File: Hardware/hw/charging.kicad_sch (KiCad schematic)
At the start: 7 parts, among them J1 Screw_Terminal_01x02, J2 Screw_Terminal_01x02, Q2 PMOS, Q3 PMOS, U3 INA219, U7 BQ24650

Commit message: Scheme update
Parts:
- added Q4: PMOS, symbol Simulation_SPICE:PMOS
- added R3: 100k, symbol Device:R
- added R4: 1k, symbol Device:R
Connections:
- net at Q3.3 (S): now also Q4.3 (S), R3.1
- new net: Q4.2 (G), R3.2, R4.1
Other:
- moved on the sheet: U3

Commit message: update
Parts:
- removed U3: INA219, INA219:MODULE_INA219, symbol INA219:INA219
- removed U7: BQ24650, symbol BQ24650:BQ24650
- added J3: Conn_01x05_Pin, Connector_PinSocket_2.54mm:PinSocket_1x05_P2.54mm_Vertical, symbol Connector:Conn_01x05_Pin
- added J5: Conn_01x04_Pin, Connector_PinSocket_2.54mm:PinSocket_1x04_P2.54mm_Vertical, symbol Connector:Conn_01x04_Pin
- added R5, R6: 4k7, symbol Device:R
- added R7, R8: 10k, symbol Device:R
- added SunnyBuddy:PRT-12885: ~, SunnyBuddy:PRT-12885, symbol PRT-12885:Sunny Buddy PRT-12885
- added U3, U8: SMS3.3.TCT, symbol DVIULC6-4SC6:SMS3.3.TCT
- added U7: INA219, INA219_Module:MODULE_INA219, symbol INA219:INA219
- D3: footprint (none) -> SMBJ24CA:DO214AA
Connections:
- net GND: now also J3.5 (Pin_5), J5.4 (Pin_4), SunnyBuddy:PRT-12885.2 (Sol-), SunnyBuddy:PRT-12885.4 (GND), U3.2 (GND), U7.2 (GND), U8.2 (GND)
- net Charging: now reaches R4.2
- net Charging: now also J3.4 (Pin_4), U3.6 (IO4)
- net at J2.1 (Pin_1): now also SunnyBuddy:PRT-12885.7 (LOAD+)
- net at J2.2 (Pin_2): now also SunnyBuddy:PRT-12885.8 (LOAD-)
- net at Q4.1 (D): now also U7.6 (VIN+)
- new net: SunnyBuddy:PRT-12885.1 (Sol+), U7.5 (VIN-)
- new net CHG: J5.3 (Pin_3), R8.2, SunnyBuddy:PRT-12885.6 (CHG), U8.6 (IO4)
- new net FAULT: J5.2 (Pin_2), R7.2, SunnyBuddy:PRT-12885.5 (FAULT), U8.3 (IO2)
- new net SCL: J3.2 (Pin_2), R5.2, U3.1 (IO1), U3.3 (IO2), U7.3 (SCL)
- new net SDA: J3.3 (Pin_3), R6.2, U7.4 (SDA)
- new net SET: J5.1 (Pin_1), SunnyBuddy:PRT-12885.3 (SET), U8.1 (IO1)
- new net VCC: J3.1 (Pin_1), R5.1, R6.1, R7.1, R8.1, U3.5 (V_{CC}), U7.1 (VCC), U8.5 (V_{CC})
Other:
- moved on the sheet: J2

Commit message: lil update
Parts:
- removed U3, U8: SMS3.3.TCT, symbol DVIULC6-4SC6:SMS3.3.TCT
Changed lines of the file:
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@@
-	)
-	(symbol
-		(lib_id "DVIULC6-4SC6:SMS3.3.TCT")
-		(at 172.72 88.9 0)
-		(unit 1)
-		(exclude_from_sim no)
-		(in_bom no)
-		(on_board no)
-		(dnp no)
-		(fields_autoplaced yes)
-		(property "Reference" "U8"
-			(at 172.085 86.36 0)
-			(effects
-				(font
-					(size 1.27 1.27)
-				)
-			)
-		)
-		(property "Value" "SMS3.3.TCT"
-			(at 172.085 88.9 0)
-			(effects
-				(font
-					(size 1.27 1.27)
-				)
-			)
-		)
-		(property "Footprint" ""
-			(at 172.72 88.9 0)
-			(effects
-				(font
-					(size 1.27 1.27)
-				)
-				(hide yes)
-			)
-		)
-		(property "Datasheet" ""
-			(at 172.72 88.9 0)
-			(effects
-				(font
-					(size 1.27 1.27)
-				)
-				(hide yes)
-			)
-		)
-		(property "Description" ""
-			(at 172.72 88.9 0)
-			(effects
-				(font
-					(size 1.27 1.27)
-				)
-				(hide yes)
-			)
-		)
-		(pin "6"
-		)
-		(pin "2"
-		)
-		(pin "3"
-		)
-		(pin "4"
-		)
-		(pin "5"
-		)
-		(pin "1"
-		)
-		(instances
-			(project ""
-				(path "/e8888c0f-4960-4960-b96f-1ca6e03d7c29/cafc10db-934b-4e35-adb4-dd7509107608"
-					(reference "U8")
-					(unit 1)
-				)
-			)
-		)
 	)
 	(symbol
@@
 					(unit 1)
 				)
-			)
-		)
-	)
-	(symbol
-		(lib_id "DVIULC6-4SC6:SMS3.3.TCT")
-		(at 106.68 88.9 0)
-		(unit 1)
-		(exclude_from_sim no)
-		(in_bom no)
-		(on_board no)
-		(dnp no)
-		(fields_autoplaced yes)
-		(property "Reference" "U3"
-			(at 106.045 86.36 0)
-			(effects
-				(font
-					(size 1.27 1.27)
-				)
-			)
-		)
-		(property "Value" "SMS3.3.TCT"
-			(at 106.045 88.9 0)
-			(effects
-				(font
-					(size 1.27 1.27)
-				)
-			)
-		)
-		(property "Footprint" ""
-			(at 106.68 88.9 0)
-			(effects
-				(font
-					(size 1.27 1.27)
-				)
-				(hide yes)
-			)
-		)
-		(property "Datasheet" ""
-			(at 106.68 88.9 0)
-			(effects
-				(font
-					(size 1.27 1.27)
-				)
-				(hide yes)
-			)
-		)
-		(property "Description" ""
-			(at 106.68 88.9 0)
-			(effects
-				(font
-					(size 1.27 1.27)
-				)
-				(hide yes)
-			)
-		)
-		(pin "4"
-		)
-		(pin "3"
-		)
-		(pin "5"
-		)
-		(pin "6"
-		)
-		(pin "1"
-		)
-		(pin "2"
-		)
-		(instances
-			(project ""
-				(path "/e8888c0f-4960-4960-b96f-1ca6e03d7c29/cafc10db-934b-4e35-adb4-dd7509107608"
-					(reference "U3")
-					(unit 1)
-				)

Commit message: SMS3.3.TCT update
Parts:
- added R10, R9: 10k, symbol Device:R
- added U3, U8: SMS3.3.TCT, SC-59-6 (SOT-23-6), symbol SMS3.3:_1
- SunnyBuddy:PRT-12885: footprint SunnyBuddy:PRT-12885 -> SunnyBuddy:Untitled
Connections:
- net CHG: now also R10.1, U8.4 (IO2)
- net Charging: now also U3.4 (IO2)
- net FAULT: now also R9.1, U8.3 (IO3)
- net GND: now also U3.2 (GND), U3.5 (GND), U8.2 (GND), U8.5 (GND)
- net SCL: now also U3.1 (IO1), U3.3 (IO3)
- net SET: now also U8.1 (IO1)
- net VCC: now also R10.2, R9.2

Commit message: scheme update
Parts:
- added C6: 100n, Capacitor_SMD:C_0805_2012Metric, symbol Device:C
- added C7: 470u, Capacitor_THT:CP_Radial_D10.0mm_P5.00mm, symbol Device:C_Polarized
- Q2, Q3, Q4: footprint (none) -> PMOS-SOT23:PMOS-SOT23
- R10, R3, R4, R5, R6, R7, R8, R9: footprint (none) -> Resistor_SMD:R_0805_2012Metric
- SunnyBuddy:PRT-12885: footprint SunnyBuddy:Untitled -> SunnyBuddy:PRT-12885
- U3, U8: footprint SC-59-6 (SOT-23-6) -> MyESDProtection:SMS3.3.TCT
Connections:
- net GND: now also D3.1, C6.2, C7.2; no longer D3.2
- net SCL: no longer U3.3 (IO3)
- net SDA: now also U3.3 (IO3)
- net at J1.2 (Pin_2), Q2.3 (S): now also D3.2, C7.1; no longer D3.1
- net at Q4.1 (D), U7.6 (VIN+): now also C6.1
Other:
- moved on the sheet: D3, J1, J2, Q2, Q3, Q4, R3, R4, SunnyBuddy:PRT-12885, U7

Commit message: IoT board update
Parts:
- added Q5: NMOS, symbol Simulation_SPICE:NMOS
- R10: value 10k -> 220
- R4: value 1k -> 220
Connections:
- net CHG: no longer R10.1
- net Charging: now also R10.1; no longer R4.2
- net FAULT: no longer R9.1
- net GND: now also R9.2, Q5.3 (S)
- net VCC: no longer R10.2, R9.2
- new net: Q5.1 (D), R4.2
- new net: Q5.2 (G), R10.2, R9.1
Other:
- moved on the sheet: J3, J5, R4, R5, R6, R7, R8, U3, U8

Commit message: IoT update
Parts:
- removed J2: Screw_Terminal_01x02, TerminalBlock_Phoenix:TerminalBlock_Phoenix_MPT-0,5-2-2.54_1x02_P2.54mm_Horizontal, symbol Connector:Screw_Terminal_01x02
- removed J3: Conn_01x05_Pin, Connector_PinSocket_2.54mm:PinSocket_1x05_P2.54mm_Vertical, symbol Connector:Conn_01x05_Pin
- removed J5: Conn_01x04_Pin, Connector_PinSocket_2.54mm:PinSocket_1x04_P2.54mm_Vertical, symbol Connector:Conn_01x04_Pin
- removed R5, R6: 4k7, Resistor_SMD:R_0805_2012Metric, symbol Device:R
- removed R7, R8: 10k, Resistor_SMD:R_0805_2012Metric, symbol Device:R
- removed SunnyBuddy:PRT-12885: ~, SunnyBuddy:PRT-12885, symbol PRT-12885:Sunny Buddy PRT-12885
- removed U3, U8: SMS3.3.TCT, MyESDProtection:SMS3.3.TCT, symbol SMS3.3:_1
- added R1, R16: 4k7, Resistor_SMD:R_0805_2012Metric, symbol Device:R
- added R19, R20: 10k, Resistor_SMD:R_0805_2012Metric, symbol Device:R
- added U4: SunnyBuddy:PRT-12885, SunnyBuddy:PRT-12885, symbol PRT-12885:Sunny Buddy PRT-12885
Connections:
- net CHG: now also R20.2, U4.6 (CHG)
- net FAULT: now also R19.2, U4.5 (FAULT)
- net GND: now also U4.2 (Sol-), U4.4 (GND), U4.8 (LOAD-)
- net SET: now also U4.3 (SET)
- net at U7.5 (VIN-): now also U4.1 (Sol+)
- net Charging renamed GPIO21
- net SCL renamed I2C_SCL
- net I2C_SCL: now also R1.2
- net SDA renamed I2C_SDA
- net I2C_SDA: now also R16.2
- net VCC renamed 3v3
- net 3v3: now also R1.1, R16.1, R19.1, R20.1
- new net Load: U4.7 (LOAD+)

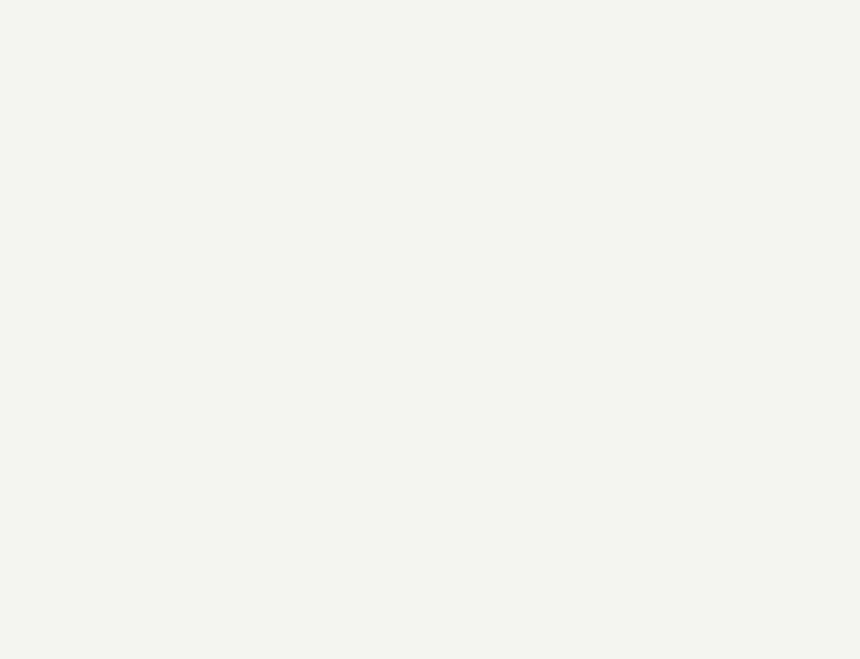
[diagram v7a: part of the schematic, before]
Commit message: USB and UART update
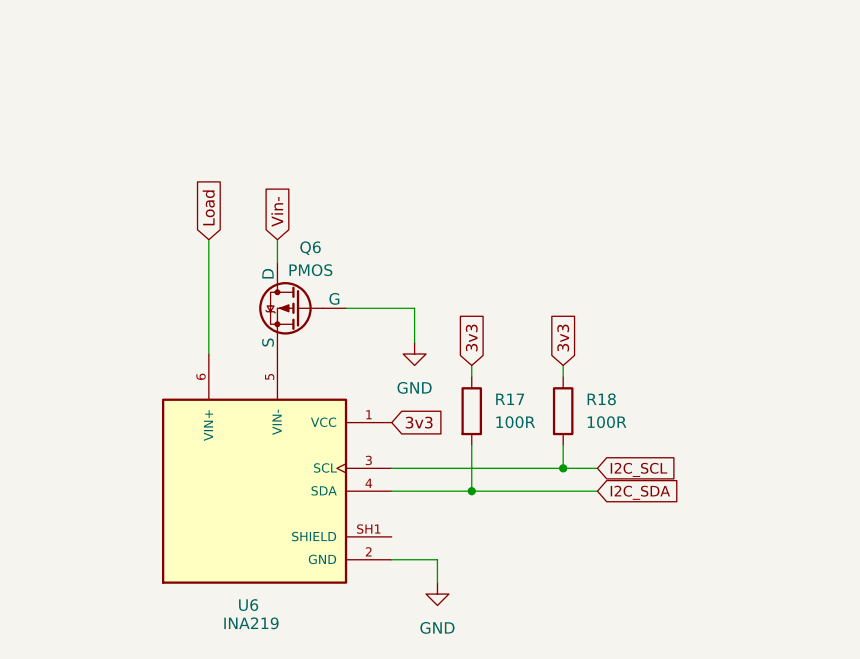
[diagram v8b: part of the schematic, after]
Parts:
- added Q6: PMOS, PMOS-SOT23:PMOS-SOT23, symbol Simulation_SPICE:PMOS
- added R17, R18: 100R, Resistor_SMD:R_0805_2012Metric, symbol Device:R
- added U6: INA219, INA219_Module:MODULE_INA219, symbol INA219:INA219
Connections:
- net 3v3: now also R17.1, R18.1, U6.1 (VCC)
- net GND: now also Q6.2 (G), U6.2 (GND)
- net I2C_SCL: now also R18.2, U6.3 (SCL)
- net I2C_SDA: now also R17.2, U6.4 (SDA)
- net Load: now also U6.6 (VIN+)
- new net: Q6.3 (S), U6.5 (VIN-)
- new net Vin-: Q6.1 (D)
